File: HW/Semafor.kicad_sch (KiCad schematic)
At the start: 65 parts, among them J1 USB_C_Receptacle_USB2.0, J2 USB_plug, M1 Motor_DC, Q3 Q_NMOS_GSD, Q4 Q_NMOS_GSD, SW6 SW_SPDT, U1 ESP32-C3, U2 CN3058E, U3 LT1930, U4 E22-900T22D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

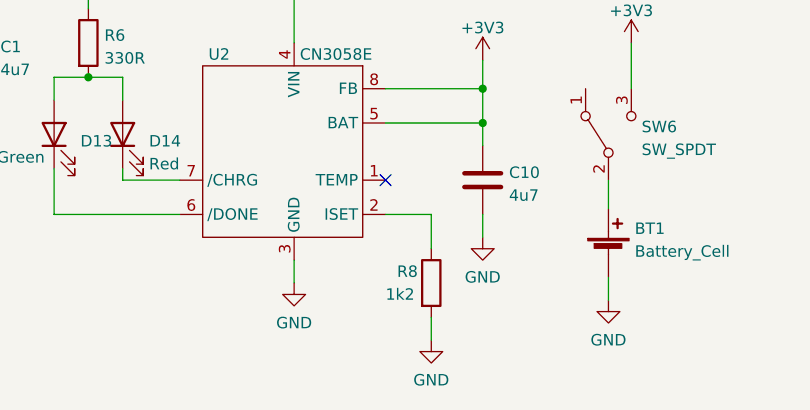
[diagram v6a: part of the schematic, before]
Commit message: add datasheet, change engagement at CN3058E of TEMP
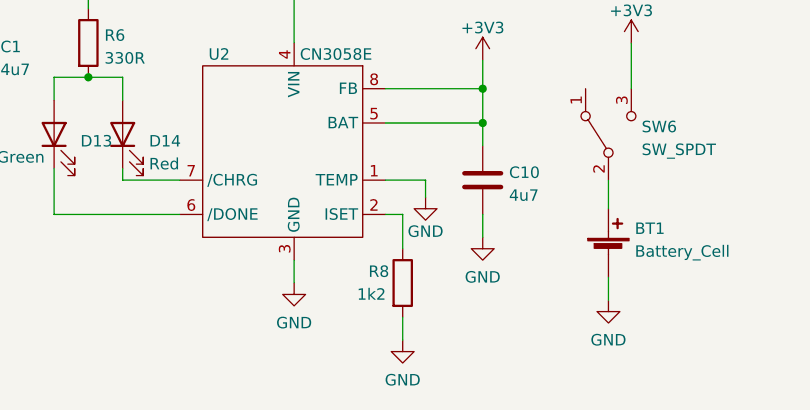
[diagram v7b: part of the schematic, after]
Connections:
- net GND: now also U2.1 (TEMP)
- no-connect marks 11 -> 10
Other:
- moved on the sheet: R8
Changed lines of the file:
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@@
   )
   (no_connect (at 34.29 172.72))
-  (no_connect (at 113.03 171.45))
   (no_connect (at 278.13 60.96))
   (no_connect (at 158.75 41.91))
@@
   (no_connect (at 144.78 102.87))
   (no_connect (at 25.4 142.24))
-  (wire (pts (xy 118.11 186.69) (xy 118.11 189.23))
+  (wire (pts (xy 114.935 186.69) (xy 114.935 189.23))
     (stroke (width 0) (type default) (color 0 0 0 0))
   )
@@
     (stroke (width 0) (type default) (color 0 0 0 0))
   )
+  (wire (pts (xy 117.475 173.355) (xy 117.475 171.45))
+    (stroke (width 0) (type default) (color 0 0 0 0))
+  )
   (wire (pts (xy 87.63 118.11) (xy 87.63 120.015))
     (stroke (width 0) (type default) (color 0 0 0 0))
@@
     (stroke (width 0) (type default) (color 0 0 0 0))
   )
-  (wire (pts (xy 113.03 175.26) (xy 118.11 175.26))
+  (wire (pts (xy 113.03 175.26) (xy 114.935 175.26))
     (stroke (width 0) (type default) (color 0 0 0 0))
   )
@@
     (stroke (width 0) (type default) (color 0 0 0 0))
   )
+  (wire (pts (xy 113.03 171.45) (xy 117.475 171.45))
+    (stroke (width 0) (type default) (color 0 0 0 0))
+  )
   (wire (pts (xy 156.21 124.46) (xy 156.21 125.73))
     (stroke (width 0) (type default) (color 0 0 0 0))
@@
     (stroke (width 0) (type default) (color 0 0 0 0))
   )
-  (wire (pts (xy 118.11 175.26) (xy 118.11 179.07))
+  (wire (pts (xy 114.935 175.26) (xy 114.935 179.07))
     (stroke (width 0) (type default) (color 0 0 0 0))
   )
@@
     (pin "1")
   )
+  (symbol (lib_id "power:GND") (at 117.475 173.355 0) (unit 1)
+    (in_bom yes) (on_board yes)
+    (property "Reference" "#PWR?" (id 0) (at 117.475 179.705 0)
+      (effects (font (size 1.27 1.27)) hide)
+    )
+    (property "Value" "GND" (id 1) (at 117.475 177.165 0))
+    (property "Footprint" "" (id 2) (at 117.475 173.355 0)
+      (effects (font (size 1.27 1.27)) hide)
+    )
+    (property "Datasheet" "" (id 3) (at 117.475 173.355 0)
+      (effects (font (size 1.27 1.27)) hide)
+    )
+    (pin "1")
+  )
   (symbol (lib_id "power:GND") (at 191.77 156.21 0) (unit 1)
     (in_bom yes) (on_board yes) (fields_autoplaced)
@@
       (effects (font (size 1.27 1.27)) hide)
     )
-    (property "Datasheet" "" (id 3) (at 102.87 168.91 0)
+    (property "Datasheet" "http://www.consonance-elec.com/en/static/upload/file/20220425/1650867856106004.pdf" (id 3) (at 102.87 168.91 0)
       (effects (font (size 1.27 1.27)) hide)
     )
@@
     (pin "1")
   )
-  (symbol (lib_id "power:GND") (at 118.11 189.23 0) (unit 1)
+  (symbol (lib_id "power:GND") (at 114.935 189.23 0) (unit 1)
     (in_bom yes) (on_board yes) (fields_autoplaced)
-    (property "Reference" "#PWR0148" (id 0) (at 118.11 195.58 0)
+    (property "Reference" "#PWR0148" (id 0) (at 114.935 195.58 0)
       (effects (font (size 1.27 1.27)) hide)
     )
-    (property "Value" "GND" (id 1) (at 118.11 193.6734 0))
-    (property "Footprint" "" (id 2) (at 118.11 189.23 0)
+    (property "Value" "GND" (id 1) (at 114.935 193.6734 0))
+    (property "Footprint" "" (id 2) (at 114.935 189.23 0)
       (effects (font (size 1.27 1.27)) hide)
     )
-    (property "Datasheet" "" (id 3) (at 118.11 189.23 0)
+    (property "Datasheet" "" (id 3) (at 114.935 189.23 0)
       (effects (font (size 1.27 1.27)) hide)
     )
@@
     (pin "2")
   )
-  (symbol (lib_id "Device:R") (at 118.11 182.88 0) (unit 1)
+  (symbol (lib_id "Device:R") (at 114.935 182.88 0) (unit 1)
     (in_bom yes) (on_board yes)
-    (property "Reference" "R8" (id 0) (at 114.3 181.61 0)
+    (property "Reference" "R8" (id 0) (at 111.125 181.61 0)
       (effects (font (size 1.27 1.27)) (justify left))
     )
-    (property "Value" "1k2" (id 1) (at 113.03 184.15 0)
+    (property "Value" "1k2" (id 1) (at 109.855 184.15 0)
       (effects (font (size 1.27 1.27)) (justify left))
     )
-    (property "Footprint" "Resistor_SMD:R_0603_1608Metric" (id 2) (at 116.332 182.88 90)
+    (property "Footprint" "Resistor_SMD:R_0603_1608Metric" (id 2) (at 113.157 182.88 90)
       (effects (font (size 1.27 1.27)) hide)
     )
-    (property "Datasheet" "~" (id 3) (at 118.11 182.88 0)
+    (property "Datasheet" "~" (id 3) (at 114.935 182.88 0)
       (effects (font (size 1.27 1.27)) hide)
     )
@@
       (reference "#PWR0190") (unit 1) (value "+3V3") (footprint "")
     )
+    (path "/3e04f5ea-6468-499a-a678-8bc9f1e199dd"
+      (reference "#PWR?") (unit 1) (value "GND") (footprint "")
+    )
     (path "/dc51458a-51c3-4e6e-b128-98c3847d175f"

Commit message: repair shottky diodes
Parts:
- D21, D22, D23, D24: LCSC C8598 -> C2909923
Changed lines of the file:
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@@
       (effects (font (size 1.27 1.27)) hide)
     )
-    (property "Datasheet" "https://datasheet.lcsc.com/lcsc/1809140216_Jiangsu-Changjing-Electronics-Technology-Co---Ltd--B5819W-SL_C8598.pdf" (id 3) (at 40.64 167.64 0)
+    (property "Datasheet" "https://datasheet.lcsc.com/lcsc/2110281130_KUU-B5817W_C2909923.pdf" (id 3) (at 40.64 167.64 0)
       (effects (font (size 1.27 1.27)) hide)
     )
-    (property "LCSC" "C8598" (id 4) (at 40.64 167.64 0)
+    (property "LCSC" "C2909923" (id 4) (at 40.64 167.64 0)
       (effects (font (size 1.27 1.27)) hide)
     )
@@
       (effects (font (size 1.27 1.27)) hide)
     )
-    (property "Datasheet" "https://datasheet.lcsc.com/lcsc/1809140216_Jiangsu-Changjing-Electronics-Technology-Co---Ltd--B5819W-SL_C8598.pdf" (id 3) (at 54.61 104.14 0)
+    (property "Datasheet" "https://datasheet.lcsc.com/lcsc/2110281130_KUU-B5817W_C2909923.pdf" (id 3) (at 54.61 104.14 0)
       (effects (font (size 1.27 1.27)) hide)
     )
-    (property "LCSC" "C8598" (id 4) (at 54.61 104.14 0)
+    (property "LCSC" "C2909923" (id 4) (at 54.61 104.14 0)
       (effects (font (size 1.27 1.27)) hide)
     )
@@
       (effects (font (size 1.27 1.27)) hide)
     )
-    (property "Datasheet" "https://datasheet.lcsc.com/lcsc/1809140216_Jiangsu-Changjing-Electronics-Technology-Co---Ltd--B5819W-SL_C8598.pdf" (id 3) (at 34.925 33.02 0)
+    (property "Datasheet" "https://datasheet.lcsc.com/lcsc/2110281130_KUU-B5817W_C2909923.pdf" (id 3) (at 34.925 33.02 0)
       (effects (font (size 1.27 1.27)) hide)
     )
-    (property "LCSC" "C8598" (id 4) (at 34.925 33.02 0)
+    (property "LCSC" "C2909923" (id 4) (at 34.925 33.02 0)
       (effects (font (size 1.27 1.27)) hide)
     )
@@
       (effects (font (size 1.27 1.27)) hide)
     )
-    (property "Datasheet" "https://datasheet.lcsc.com/lcsc/1809140216_Jiangsu-Changjing-Electronics-Technology-Co---Ltd--B5819W-SL_C8598.pdf" (id 3) (at 76.2 33.02 0)
+    (property "Datasheet" "https://datasheet.lcsc.com/lcsc/2110281130_KUU-B5817W_C2909923.pdf" (id 3) (at 76.2 33.02 0)
       (effects (font (size 1.27 1.27)) hide)
     )
-    (property "LCSC" "C8598" (id 4) (at 76.2 33.02 0)
+    (property "LCSC" "C2909923" (id 4) (at 76.2 33.02 0)
       (effects (font (size 1.27 1.27)) hide)
     )
